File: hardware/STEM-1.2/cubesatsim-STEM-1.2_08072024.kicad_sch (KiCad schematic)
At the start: 48 parts, among them J1 Conn_02x20_Odd_Even, J2 Conn_01x04, J23 Conn_01x04, U3 MPU6050, U4 BME280, U5 YAAJ_BlackPill

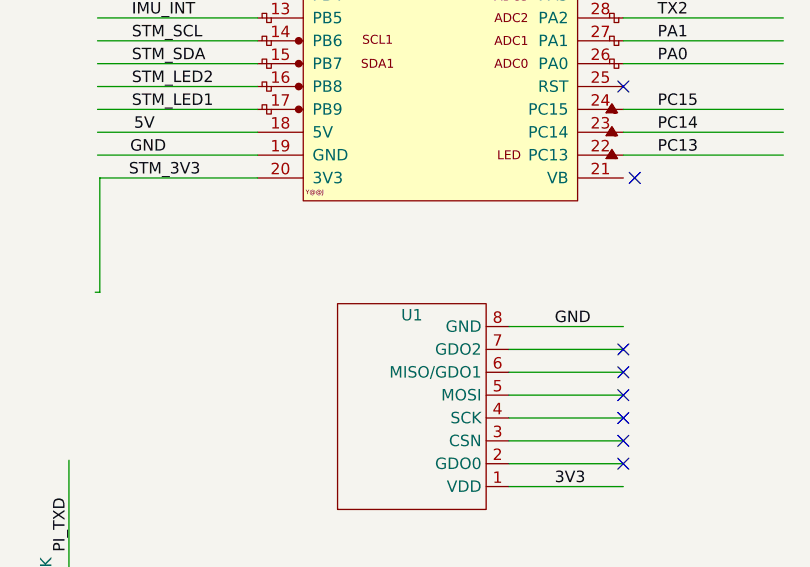
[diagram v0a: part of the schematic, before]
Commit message: Add 'DNI-CC1101' for U1.
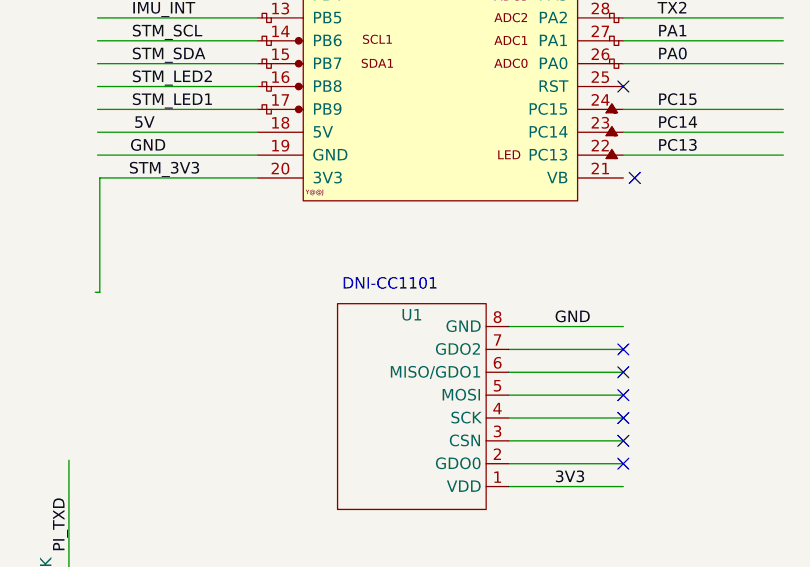
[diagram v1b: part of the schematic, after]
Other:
- note added: "DNI-CC1101"
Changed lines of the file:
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@@
+    (effects (font (size 1.27 1.27)) (justify left bottom))
+  )
+  (text "DNI-CC1101" (at 109.728 97.79 0)
     (effects (font (size 1.27 1.27)) (justify left bottom))
   )
